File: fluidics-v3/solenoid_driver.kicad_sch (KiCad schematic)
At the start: 3 parts, among them J5 Screw_Terminal_01x02, J6 Screw_Terminal_01x02, U1 TPL7407LDR

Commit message: Swap 2x terminal blocks MKDS-1,5-2-5.08 -> MPT-0,5-2-2.54
Replace two 1x02 Phoenix terminal blocks with the smaller MPT series
(2.54mm pitch, 5.54x6.20mm body vs 10.16x9.80mm) to reclaim board space.
Schematic + PCB updated; DRC parity 0. Note: MPT rated for 0.5mm2 wire
(vs 1.5mm2 on MKDS) - lower current/wire-gauge capacity.

Co-Authored-By: Claude Opus 4.8 (1M context) <noreply@anthropic.com>
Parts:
- J5, J6: footprint TerminalBlock_Phoenix:TerminalBlock_Phoenix_MKDS-1,5-2-5.08_1x02_P5.08mm_Horizontal -> TerminalBlock_Phoenix:TerminalBlock_Phoenix_MPT-0,5-2-2.54_1x02_P2.54mm_Horizontal
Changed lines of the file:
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@@
 			)
 		)
-		(property "Footprint" "TerminalBlock_Phoenix:TerminalBlock_Phoenix_MKDS-1,5-2-5.08_1x02_P5.08mm_Horizontal"
+		(property "Footprint" "TerminalBlock_Phoenix:TerminalBlock_Phoenix_MPT-0,5-2-2.54_1x02_P2.54mm_Horizontal"
 			(at 204.47 77.47 0)
 			(hide yes)
@@
 			)
 		)
-		(property "Footprint" "TerminalBlock_Phoenix:TerminalBlock_Phoenix_MKDS-1,5-2-5.08_1x02_P5.08mm_Horizontal"
+		(property "Footprint" "TerminalBlock_Phoenix:TerminalBlock_Phoenix_MPT-0,5-2-2.54_1x02_P2.54mm_Horizontal"
 			(at 204.47 87.63 0)
 			(hide yes)

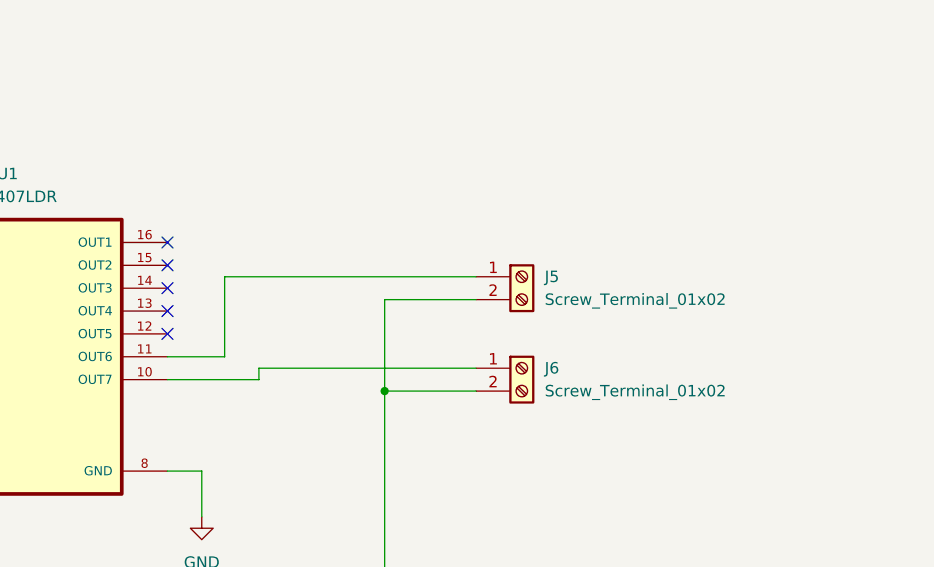
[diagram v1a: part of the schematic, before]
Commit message: Add GPIO_5 status LED and +24V screw terminal J7
- Root sheet: GPIO_5 status LED (D12 + R12 2.7K to GND)
- Solenoid driver sheet: J7 2-pin screw terminal (pin2 = +24V)

Schematic parses clean via kicad-cli; D12/R12/J7 present in netlist.

Co-Authored-By: Claude Opus 4.8 (1M context) <noreply@anthropic.com>
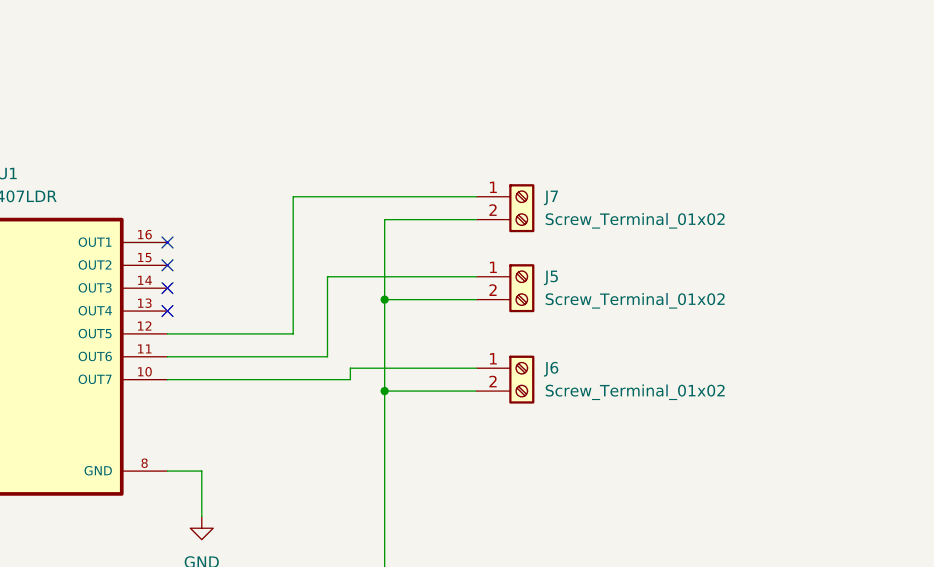
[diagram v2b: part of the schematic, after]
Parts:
- added J7: Screw_Terminal_01x02, TerminalBlock_Phoenix:TerminalBlock_Phoenix_MPT-0,5-2-2.54_1x02_P2.54mm_Horizontal, symbol Connector:Screw_Terminal_01x02
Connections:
- net +24V: now also J7.2 (Pin_2)
- net at U1.12 (OUT5): now also J7.1 (Pin_1)
- no-connect marks 5 -> 4
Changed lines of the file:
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@@
+	)
+	(junction
+		(at 189.23 80.01)
+		(diameter 0)
+		(color 0 0 0 0)
 	)
 	(junction
@@
 		(at 165.1 81.28)
 	)
-	(no_connect
-		(at 165.1 83.82)
-	)
-	(wire
-		(pts
-			(xy 189.23 90.17) (xy 189.23 80.01)
+	(wire
+		(pts
+			(xy 179.07 83.82) (xy 179.07 68.58)
+		)
+		(stroke
+			(width 0)
+			(type default)
+		)
+	)
+	(wire
+		(pts
+			(xy 182.88 77.47) (xy 199.39 77.47)
 		)
 		(stroke
@@
 	(wire
 		(pts
+			(xy 165.1 83.82) (xy 179.07 83.82)
+		)
+		(stroke
+			(width 0)
+			(type default)
+		)
+	)
+	(wire
+		(pts
 			(xy 189.23 111.76) (xy 189.23 90.17)
 		)
@@
 	(wire
 		(pts
-			(xy 165.1 88.9) (xy 175.26 88.9)
-		)
-		(stroke
-			(width 0)
-			(type default)
-		)
-	)
-	(wire
-		(pts
-			(xy 171.45 77.47) (xy 199.39 77.47)
+			(xy 179.07 68.58) (xy 199.39 68.58)
+		)
+		(stroke
+			(width 0)
+			(type default)
+		)
+	)
+	(wire
+		(pts
+			(xy 185.42 88.9) (xy 185.42 87.63)
+		)
+		(stroke
+			(width 0)
+			(type default)
+		)
+	)
+	(wire
+		(pts
+			(xy 165.1 88.9) (xy 185.42 88.9)
 		)
 		(stroke
@@
 	(wire
 		(pts
-			(xy 165.1 86.36) (xy 171.45 86.36)
+			(xy 189.23 71.12) (xy 189.23 80.01)
+		)
+		(stroke
+			(width 0)
+			(type default)
+		)
+	)
+	(wire
+		(pts
+			(xy 165.1 86.36) (xy 182.88 86.36)
 		)
 		(stroke
@@
 	(wire
 		(pts
-			(xy 171.45 86.36) (xy 171.45 77.47)
-		)
-		(stroke
-			(width 0)
-			(type default)
-		)
-	)
-	(wire
-		(pts
-			(xy 175.26 88.9) (xy 175.26 87.63)
+			(xy 199.39 71.12) (xy 189.23 71.12)
+		)
+		(stroke
+			(width 0)
+			(type default)
+		)
+	)
+	(wire
+		(pts
+			(xy 182.88 86.36) (xy 182.88 77.47)
 		)
 		(stroke
@@
 	(wire
 		(pts
-			(xy 175.26 87.63) (xy 199.39 87.63)
-		)
-		(stroke
-			(width 0)
-			(type default)
-		)
-	)
-	(wire
-		(pts
 			(xy 128.27 93.98) (xy 127 93.98)
 		)
@@
 	(wire
 		(pts
+			(xy 189.23 80.01) (xy 189.23 90.17)
+		)
+		(stroke
+			(width 0)
+			(type default)
+		)
+	)
+	(wire
+		(pts
 			(xy 0.0762 0.0762) (xy 0.0762 7.6962)
+		)
+		(stroke
+			(width 0)
+			(type default)
+		)
+	)
+	(wire
+		(pts
+			(xy 185.42 87.63) (xy 199.39 87.63)
 		)
 		(stroke
@@
 					(unit 1)
 				)
+			)
+		)
+	)
+	(symbol
+		(lib_id "Connector:Screw_Terminal_01x02")
+		(at 204.47 68.58 0)
+		(unit 1)
+		(body_style 1)
+		(exclude_from_sim no)
+		(in_bom yes)
+		(on_board yes)
+		(in_pos_files yes)
+		(dnp no)
+		(fields_autoplaced yes)
+		(property "Reference" "J7"
+			(at 207.01 68.5799 0)
+			(show_name no)
+			(do_not_autoplace no)
+			(effects
+				(font
+					(size 1.27 1.27)
+				)
+				(justify left)
+			)
+		)
+		(property "Value" "Screw_Terminal_01x02"
+			(at 207.01 71.1199 0)
+			(show_name no)
+			(do_not_autoplace no)
+			(effects
+				(font
+					(size 1.27 1.27)
+				)
+				(justify left)
+			)
+		)
+		(property "Footprint" "TerminalBlock_Phoenix:TerminalBlock_Phoenix_MPT-0,5-2-2.54_1x02_P2.54mm_Horizontal"
+			(at 204.47 68.58 0)
+			(hide yes)
+			(show_name no)
+			(do_not_autoplace no)
+			(effects
+				(font
+					(size 1.27 1.27)
+				)
+			)
+		)
+		(property "Datasheet" ""
+			(at 204.47 68.58 0)
+			(hide yes)
+			(show_name no)
+			(do_not_autoplace no)
+			(effects
+				(font
+					(size 1.27 1.27)
+				)
+			)
+		)
+		(property "Description" "Generic screw terminal, single row, 01x02, script generated (kicad-library-utils/schlib/autogen/connector/)"
+			(at 204.47 68.58 0)
+			(hide yes)
+			(show_name no)
+			(do_not_autoplace no)
+			(effects
+				(font
+					(size 1.27 1.27)
+				)
+			)
+		)
+		(pin "1"
+		)
+		(pin "2"
+		)
+		(instances
+			(project "fluidics-v2"
+				(path "/0ec91c42-8aad-437d-8c85-5e10f0e51fe0/5697258d-329e-4d0c-a016-1049d92e68d8"
+					(reference "J7")
+					(unit 1)
+				)

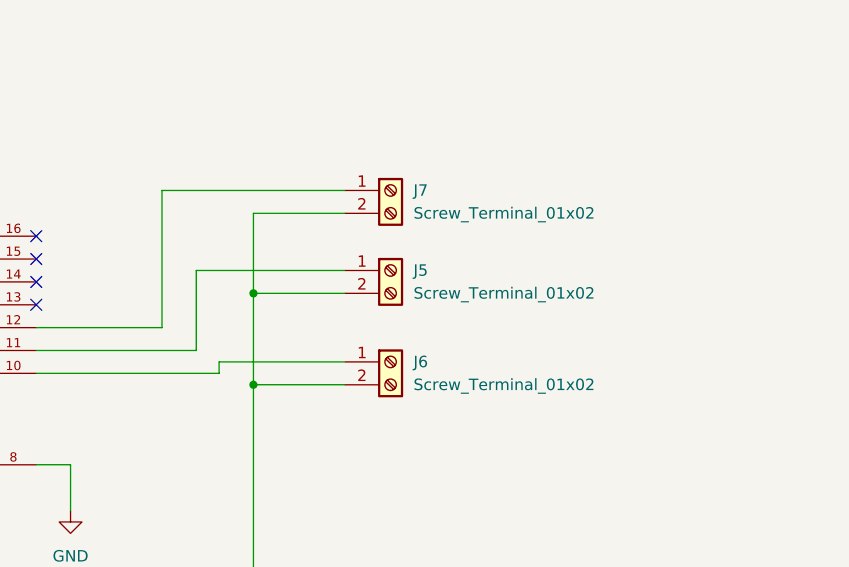
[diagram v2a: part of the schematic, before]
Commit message: Consolidate solenoid outputs to single 1x06 terminal J5
Replace 3x 1x02 blocks (J5/J6/J7) with one 6-position Xinya XY308-2.54-6P
(J5): pads 1/3/5 = U1 TPL7407 OUT5/6/7, pads 2/4/6 = +24V. DRC electrically
clean (0 clearance/shorting; 5 unconnected are intentional U2 GPIO/SPI NC).

Assign 3D model: KiCad 10 ships no Xinya XY308 .step, so point J5's model at
the bundled Phoenix MPT-0,5-6-2.54 1x06 (same pitch/positions) for the 3D
preview. Footprint/BOM/CPL still reference the real Xinya part.

Co-Authored-By: Claude Opus 4.8 (1M context) <noreply@anthropic.com>
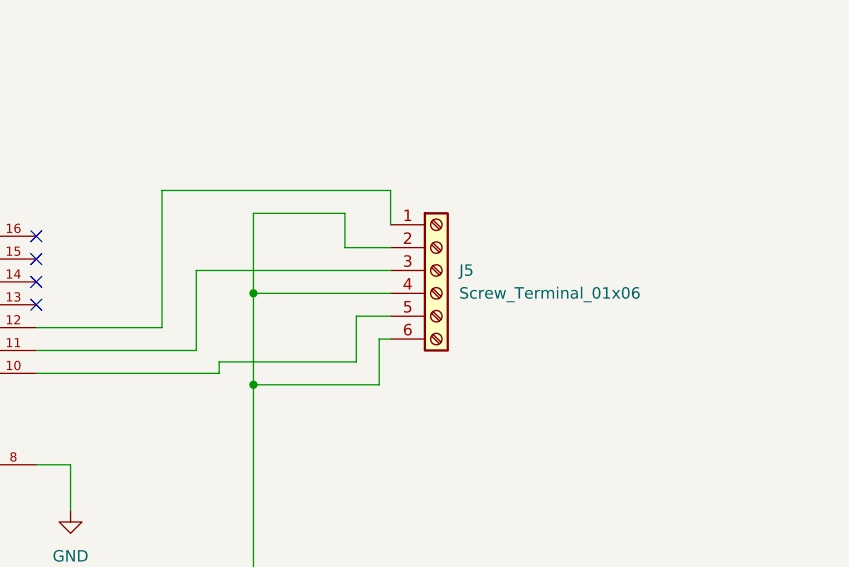
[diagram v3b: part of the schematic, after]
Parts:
- removed J5, J6, J7: Screw_Terminal_01x02, TerminalBlock_Phoenix:TerminalBlock_Phoenix_MPT-0,5-2-2.54_1x02_P2.54mm_Horizontal, symbol Connector:Screw_Terminal_01x02
- added J5: Screw_Terminal_01x06, TerminalBlock:TerminalBlock_Xinya_XY308-2.54-6P_1x06_P2.54mm_Horizontal, symbol Connector:Screw_Terminal_01x06
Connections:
- net +24V: now also J5.2 (Pin_2), J5.4 (Pin_4), J5.6 (Pin_6)
- net at U1.11 (OUT6): now also J5.3 (Pin_3)
- net at U1.10 (OUT7): now also J5.5 (Pin_5)
- net at U1.12 (OUT5): now also J5.1 (Pin_1)
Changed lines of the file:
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@@
+	(wire
+		(pts
+			(xy 203.2 85.09) (xy 204.47 85.09)
+		)
+		(stroke
+			(width 0)
+			(type default)
+		)
+	)
+	(wire
+		(pts
+			(xy 203.2 90.17) (xy 203.2 85.09)
+		)
+		(stroke
+			(width 0)
+			(type default)
+		)
+	)
 	(wire
 		(pts
@@
 	(wire
 		(pts
-			(xy 182.88 77.47) (xy 199.39 77.47)
-		)
-		(stroke
-			(width 0)
-			(type default)
-		)
-	)
-	(wire
-		(pts
-			(xy 189.23 80.01) (xy 199.39 80.01)
+			(xy 182.88 77.47) (xy 204.47 77.47)
+		)
+		(stroke
+			(width 0)
+			(type default)
+		)
+	)
+	(wire
+		(pts
+			(xy 189.23 80.01) (xy 204.47 80.01)
 		)
 		(stroke
@@
 	(wire
 		(pts
+			(xy 200.66 87.63) (xy 200.66 82.55)
+		)
+		(stroke
+			(width 0)
+			(type default)
+		)
+	)
+	(wire
+		(pts
+			(xy 200.66 82.55) (xy 204.47 82.55)
+		)
+		(stroke
+			(width 0)
+			(type default)
+		)
+	)
+	(wire
+		(pts
+			(xy 204.47 68.58) (xy 204.47 72.39)
+		)
+		(stroke
+			(width 0)
+			(type default)
+		)
+	)
+	(wire
+		(pts
 			(xy 189.23 111.76) (xy 189.23 90.17)
 		)
@@
 	(wire
 		(pts
-			(xy 179.07 68.58) (xy 199.39 68.58)
+			(xy 199.39 74.93) (xy 204.47 74.93)
+		)
+		(stroke
+			(width 0)
+			(type default)
+		)
+	)
+	(wire
+		(pts
+			(xy 199.39 71.12) (xy 199.39 74.93)
+		)
+		(stroke
+			(width 0)
+			(type default)
+		)
+	)
+	(wire
+		(pts
+			(xy 179.07 68.58) (xy 204.47 68.58)
 		)
 		(stroke
@@
 	(wire
 		(pts
-			(xy 189.23 90.17) (xy 199.39 90.17)
+			(xy 189.23 90.17) (xy 203.2 90.17)
 		)
 		(stroke
@@
 	(wire
 		(pts
-			(xy 185.42 87.63) (xy 199.39 87.63)
+			(xy 185.42 87.63) (xy 200.66 87.63)
 		)
 		(stroke
@@
 	)
 	(symbol
-		(lib_id "Connector:Screw_Terminal_01x02")
-		(at 204.47 77.47 0)
-		(unit 1)
-		(body_style 1)
-		(exclude_from_sim no)
-		(in_bom yes)
-		(on_board yes)
-		(in_pos_files yes)
-		(dnp no)
-		(fields_autoplaced yes)
-		(property "Reference" "J5"
-			(at 207.01 77.4699 0)
-			(show_name no)
-			(do_not_autoplace no)
-			(effects
-				(font
-					(size 1.27 1.27)
-				)
-				(justify left)
-			)
-		)
-		(property "Value" "Screw_Terminal_01x02"
-			(at 207.01 80.0099 0)
-			(show_name no)
-			(do_not_autoplace no)
-			(effects
-				(font
-					(size 1.27 1.27)
-				)
-				(justify left)
-			)
-		)
-		(property "Footprint" "TerminalBlock_Phoenix:TerminalBlock_Phoenix_MPT-0,5-2-2.54_1x02_P2.54mm_Horizontal"
-			(at 204.47 77.47 0)
-			(hide yes)
-			(show_name no)
-			(do_not_autoplace no)
-			(effects
-				(font
-					(size 1.27 1.27)
-				)
-			)
-		)
-		(property "Datasheet" ""
-			(at 204.47 77.47 0)
-			(hide yes)
-			(show_name no)
-			(do_not_autoplace no)
-			(effects
-				(font
-					(size 1.27 1.27)
-				)
-			)
-		)
-		(property "Description" "Generic screw terminal, single row, 01x02, script generated (kicad-library-utils/schlib/autogen/connector/)"
-			(at 204.47 77.47 0)
-			(hide yes)
-			(show_name no)
-			(do_not_autoplace no)
-			(effects
-				(font
-					(size 1.27 1.27)
-				)
-			)
-		)
-		(pin "1"
-		)
-		(pin "2"
-		)
-		(instances
-			(project "fluidics-v2"
-				(path "/0ec91c42-8aad-437d-8c85-5e10f0e51fe0/5697258d-329e-4d0c-a016-1049d92e68d8"
-					(reference "J5")
-					(unit 1)
-				)
-			)
-		)
-	)
-	(symbol
 		(lib_id "TPL7407LDR:TPL7407LDR")
 		(at 147.32 86.36 0)
@@
 	)
 	(symbol
-		(lib_id "Connector:Screw_Terminal_01x02")
-		(at 204.47 68.58 0)
+		(lib_id "Connector:Screw_Terminal_01x06")
+		(at 209.55 77.47 0)
 		(unit 1)
 		(body_style 1)
@@
 		(dnp no)
 		(fields_autoplaced yes)
-		(property "Reference" "J7"
-			(at 207.01 68.5799 0)
+		(property "Reference" "J5"
+			(at 212.09 77.4699 0)
 			(show_name no)
 			(do_not_autoplace no)
@@
 			)
 		)
-		(property "Value" "Screw_Terminal_01x02"
-			(at 207.01 71.1199 0)
+		(property "Value" "Screw_Terminal_01x06"
+			(at 212.09 80.0099 0)
 			(show_name no)
 			(do_not_autoplace no)
@@
 			)
 		)
-		(property "Footprint" "TerminalBlock_Phoenix:TerminalBlock_Phoenix_MPT-0,5-2-2.54_1x02_P2.54mm_Horizontal"
-			(at 204.47 68.58 0)
+		(property "Footprint" "TerminalBlock:TerminalBlock_Xinya_XY308-2.54-6P_1x06_P2.54mm_Horizontal"
+			(at 209.55 77.47 0)
 			(hide yes)
 			(show_name no)
@@
 		)
 		(property "Datasheet" ""
-			(at 204.47 68.58 0)
-			(hide yes)
-			(show_name no)
-			(do_not_autoplace no)
-			(effects
-				(font
-					(size 1.27 1.27)
-				)
-			)
-		)
-		(property "Description" "Generic screw terminal, single row, 01x02, script generated (kicad-library-utils/schlib/autogen/connector/)"
-			(at 204.47 68.58 0)
+			(at 209.55 77.47 0)
+			(hide yes)
+			(show_name no)
+			(do_not_autoplace no)
+			(effects
+				(font
+					(size 1.27 1.27)
+				)
+			)
+		)
+		(property "Description" "Generic screw terminal, single row, 01x06, script generated (kicad-library-utils/schlib/autogen/connector/)"
+			(at 209.55 77.47 0)
 			(hide yes)
 			(show_name no)
@@
 		)
 		(pin "2"
+		)
+		(pin "4"
+		)
+		(pin "6"
+		)
+		(pin "3"
+		)
+		(pin "5"
 		)
 		(instances
 			(project "fluidics-v2"
 				(path "/0ec91c42-8aad-437d-8c85-5e10f0e51fe0/5697258d-329e-4d0c-a016-1049d92e68d8"
-					(reference "J7")
+					(reference "J5")
 					(unit 1)
 				)
@@
 					(unit 1)
 				)
-			)
-		)
-	)
-	(symbol
-		(lib_id "Connector:Screw_Terminal_01x02")
-		(at 204.47 87.63 0)
-		(unit 1)
-		(body_style 1)
-		(exclude_from_sim no)
-		(in_bom yes)
-		(on_board yes)
-		(in_pos_files yes)
-		(dnp no)
-		(fields_autoplaced yes)
-		(property "Reference" "J6"
-			(at 207.01 87.6299 0)
-			(show_name no)
-			(do_not_autoplace no)
-			(effects
-				(font
-					(size 1.27 1.27)
-				)
-				(justify left)
-			)
-		)
-		(property "Value" "Screw_Terminal_01x02"
-			(at 207.01 90.1699 0)
-			(show_name no)
-			(do_not_autoplace no)
-			(effects
-				(font
-					(size 1.27 1.27)
-				)
-				(justify left)
-			)
-		)
-		(property "Footprint" "TerminalBlock_Phoenix:TerminalBlock_Phoenix_MPT-0,5-2-2.54_1x02_P2.54mm_Horizontal"
-			(at 204.47 87.63 0)
-			(hide yes)
-			(show_name no)
-			(do_not_autoplace no)
-			(effects
-				(font
-					(size 1.27 1.27)
-				)
-			)
-		)
-		(property "Datasheet" ""
-			(at 204.47 87.63 0)
-			(hide yes)
-			(show_name no)
-			(do_not_autoplace no)
-			(effects
-				(font
-					(size 1.27 1.27)
-				)
-			)
-		)
-		(property "Description" "Generic screw terminal, single row, 01x02, script generated (kicad-library-utils/schlib/autogen/connector/)"
-			(at 204.47 87.63 0)
-			(hide yes)
-			(show_name no)
-			(do_not_autoplace no)
-			(effects
-				(font
-					(size 1.27 1.27)
-				)
-			)
-		)
-		(pin "1"
-		)
-		(pin "2"
-		)
-		(instances
-			(project "fluidics-v2"
-				(path "/0ec91c42-8aad-437d-8c85-5e10f0e51fe0/5697258d-329e-4d0c-a016-1049d92e68d8"
-					(reference "J6")
-					(unit 1)
-				)

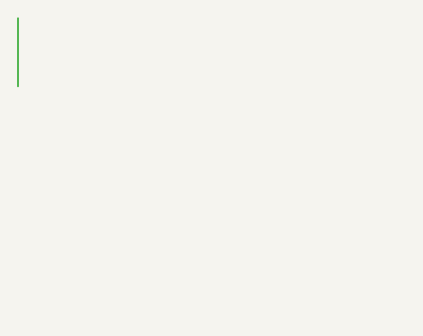
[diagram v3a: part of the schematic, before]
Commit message: v3 PCB: 3.3V power-plane islands + B.Cu bridge, refdes to F.Fab, block silk labels
PCB (this session, verified DRC-clean, 0 electrical regressions):
- Add +3.3V copper islands on In2.Cu (top U11/IC2 cluster + LDO/I2C-connector corner)
- Add +3.3V bridge pour on B.Cu down the inter-island corridor; delete ~18mm redundant vertical run
- Stitch 3.3V loads to islands with vias; remove ~35mm circuitous surface routing (3.3V trace 194->68mm)
- Move 21 hidden reference designators (caps, R22/R23/R51, U2 Teensy) to F.Fab, centered
- Add functional F.Silkscreen labels: Solenoid Driver, Flow, I2C Iso, RS-232

Also bundles accompanying schematic/library work not authored this session
(fluidics-v2.kicad_sch, svalves, solenoid_driver, 87832-0410 Molex connector lib).

Co-Authored-By: Claude Opus 4.8 (1M context) <noreply@anthropic.com>
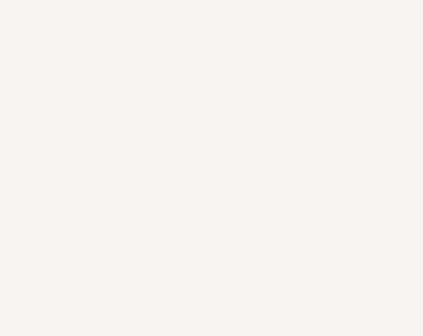
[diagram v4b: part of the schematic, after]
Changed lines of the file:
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@@
-	(wire
-		(pts
-			(xy 0.0762 0.0762) (xy 0.0762 7.6962)
-		)
-		(stroke
-			(width 0)
-			(type default)
-		)
-	)
 	(wire
 		(pts
